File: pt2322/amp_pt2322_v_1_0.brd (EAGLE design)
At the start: 50.5 x 50.8 mm, 33 parts, among them U1 PT2322-S

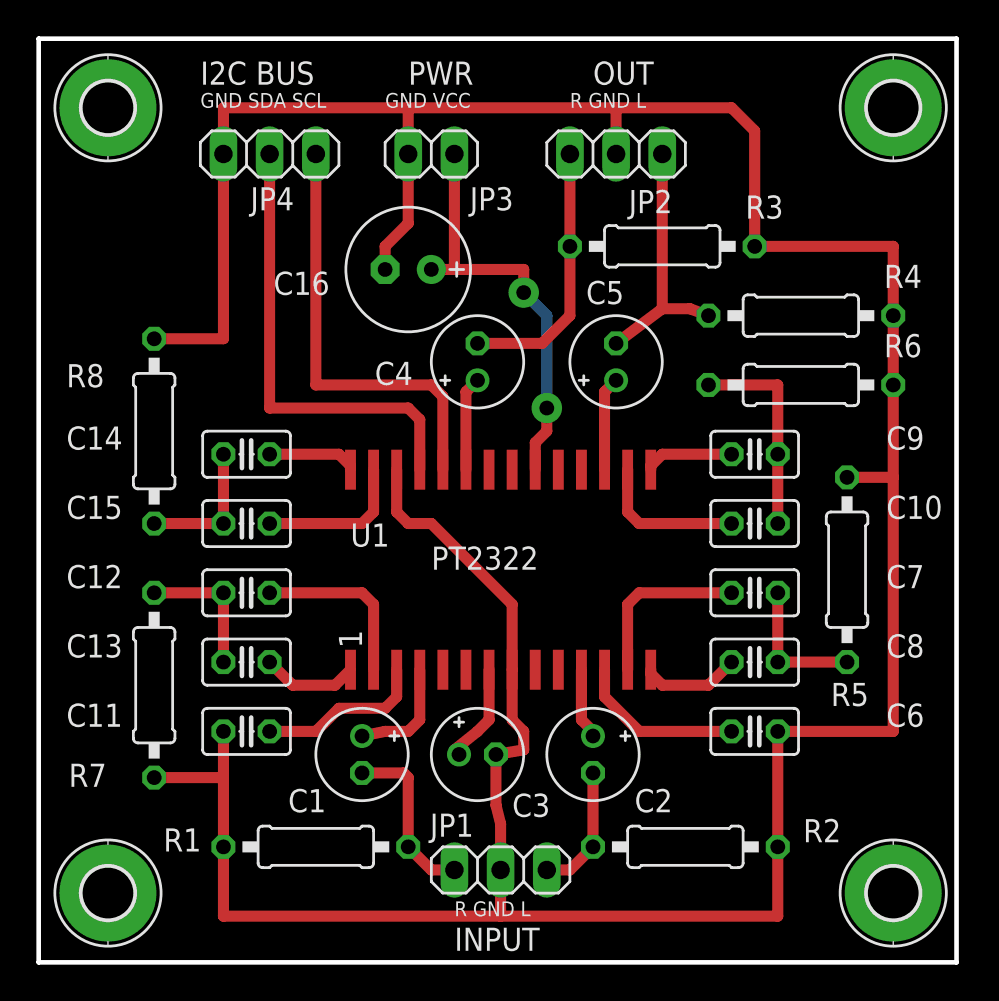
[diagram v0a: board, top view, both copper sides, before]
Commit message: Added interface board for 20x4 lcd, improved firmware for 20x4, refactored pt2322 board
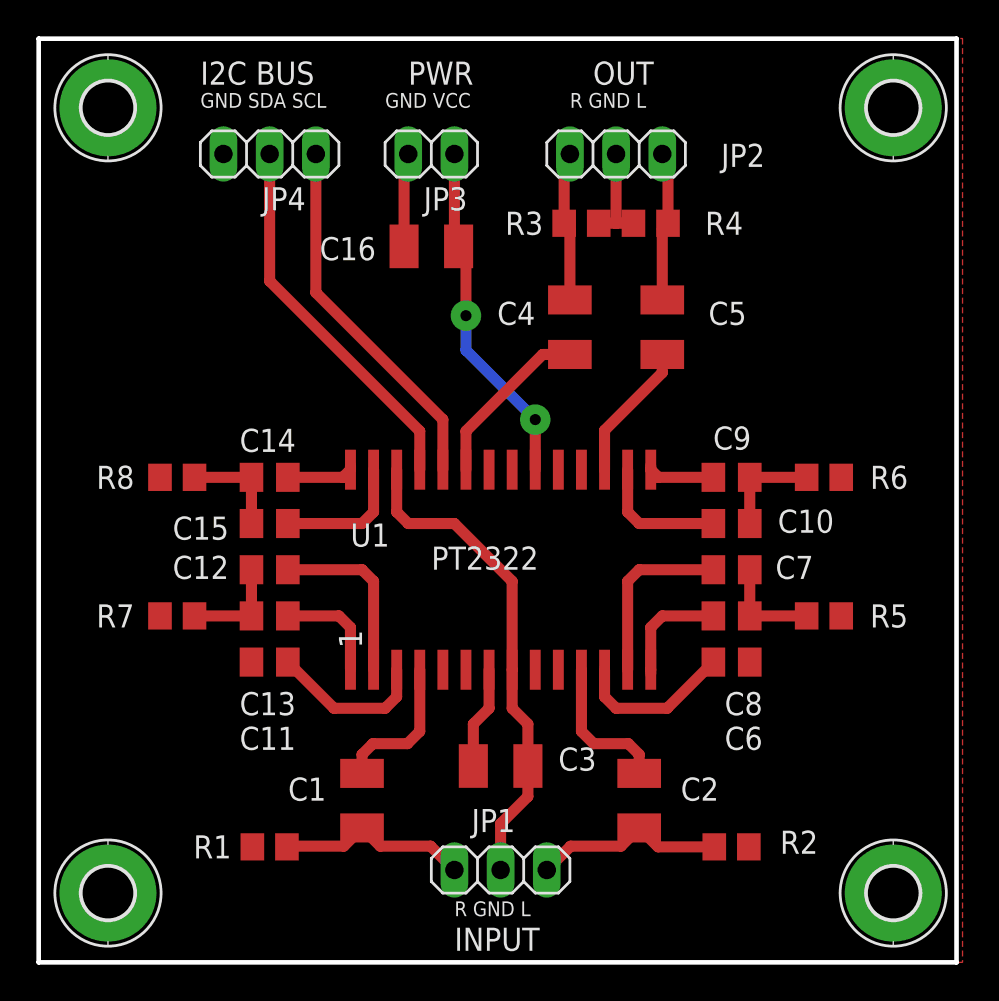
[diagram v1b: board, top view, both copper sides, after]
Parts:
- C1, C2, C3, C4, C5: device rcl:E2-5 -> rcl:SMC_B
- C10, C11, C12, C13, C14, C15, C6, C7, C8, C9: device rcl:C025-025X050 -> rcl:C0805K
- C16: device rcl:E2,5-7 -> rcl:SMC_B
- R1, R2, R3, R4, R5, R6, R7, R8: device rcl:0207/10 -> rcl:R0805
- moved R4 9.69 mm to (33.7, 40.6), turned to 180 degrees
- moved C4 5.43 mm to (29.2, 34.9)
- moved R6 5.24 mm to (43.2, 26.7)
- moved R3 4.62 mm to (29.8, 40.6)
- moved C11 4.02 mm to (12.7, 16.5)
- moved C6 4.02 mm to (38.1, 16.5)
- moved R7 4.02 mm to (7.62, 19.1), turned to 0 degrees
- moved C2 3.59 mm to (33.0, 8.89)
- moved C5 3.17 mm to (34.3, 34.9)
- moved R5 2.84 mm to (43.2, 19.1), turned to 0 degrees
- moved R8 2.84 mm to (7.62, 26.7), turned to 0 degrees
- moved C13 2.84 mm to (12.7, 19.1)
- moved C8 2.84 mm to (38.1, 19.1)
- moved R1 2.54 mm to (12.7, 6.35)
- moved C1 2.54 mm to (17.8, 8.89)
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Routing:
- net GND: track 191.9 -> 38.0 mm
- net N$23: track 14.6 -> 8.29 mm
- net N$24: track 14.3 -> 8.29 mm
- net N$12: track 11.4 -> 5.67 mm
- net N$42: track 25.2 -> 20.8 mm
- net N$21: track 5.18 -> 9.58 mm
- net VCC: track 23.2 -> 19.2 mm
- net N$2: track 4.27 -> 8.13 mm
- net N$41: track 24.0 -> 20.3 mm
- net N$4: track 7.49 -> 10.7 mm
- net N$22: track 5.18 -> 7.65 mm
- net N$16: track 7.62 -> 5.67 mm
- net N$1: track 6.22 -> 8.13 mm
- net N$20: track 7.62 -> 5.76 mm
- net N$9: track 7.62 -> 6.12 mm
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- added copper zone on layer 1, net GND
